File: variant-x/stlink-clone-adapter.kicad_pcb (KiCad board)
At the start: 2 copper layers, 25.4 x 15 mm, 5 parts, among them J1 Conn_01x04, J2 Conn_01x04, J3 2X5_HDR, J4 Conn_01x04, J5 ARM_10PIN

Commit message: variant-x plot done
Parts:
- added D1: LED, LED_SMD:LED_0603_1608Metric, F.Cu at (141.5, 117.9)
- added R1: R, Resistor_SMD:R_0603_1608Metric, F.Cu at (145.5, 117.8)
- added REF**: snowflake, project-lib:snowflake, F.Cu at (143.3, 115.3)
- moved J5 5.72 mm to (151.8, 110.5)
- moved J1 5.46 mm to (141.0, 106.7)
- moved J2 5.34 mm to (143.5, 106.7)
- moved J4 5.34 mm to (146.1, 106.7)
- moved J3 4.18 mm to (119.4, 105.4)
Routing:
- net /3.3V: track 0.00 -> 40.7 mm
- net /RST: track 0.00 -> 24.7 mm
- net /SWDIO|SWCLK: track 0.00 -> 22.6 mm
- net /GND: track 1.27 -> 21.4 mm, vias 0 -> 2
- net /GND|SWIM: track 0.00 -> 17.5 mm
- net /SWCLK: track 0.00 -> 15.6 mm
- net /GND|SWDIO: track 0.00 -> 15.5 mm
- net /SWIM: track 0.00 -> 14.0 mm
- net /SWIM|GND: track 0.00 -> 13.0 mm
- net /SWDIO: track 0.00 -> 10.8 mm
- net /SWCLK|GND: track 0.00 -> 10.5 mm
- net Net-(D1-Pad1): track 0.00 -> 2.45 mm
- added copper zone on F.Cu, net (none)
- added copper zone on B.Cu, net /GND
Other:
- board size 25.4 x 15 mm -> 25.1 x 18 mm
- board text added: "+3.3V"

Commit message: note for jumper
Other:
- board text added: "1"
- board text added: "2"

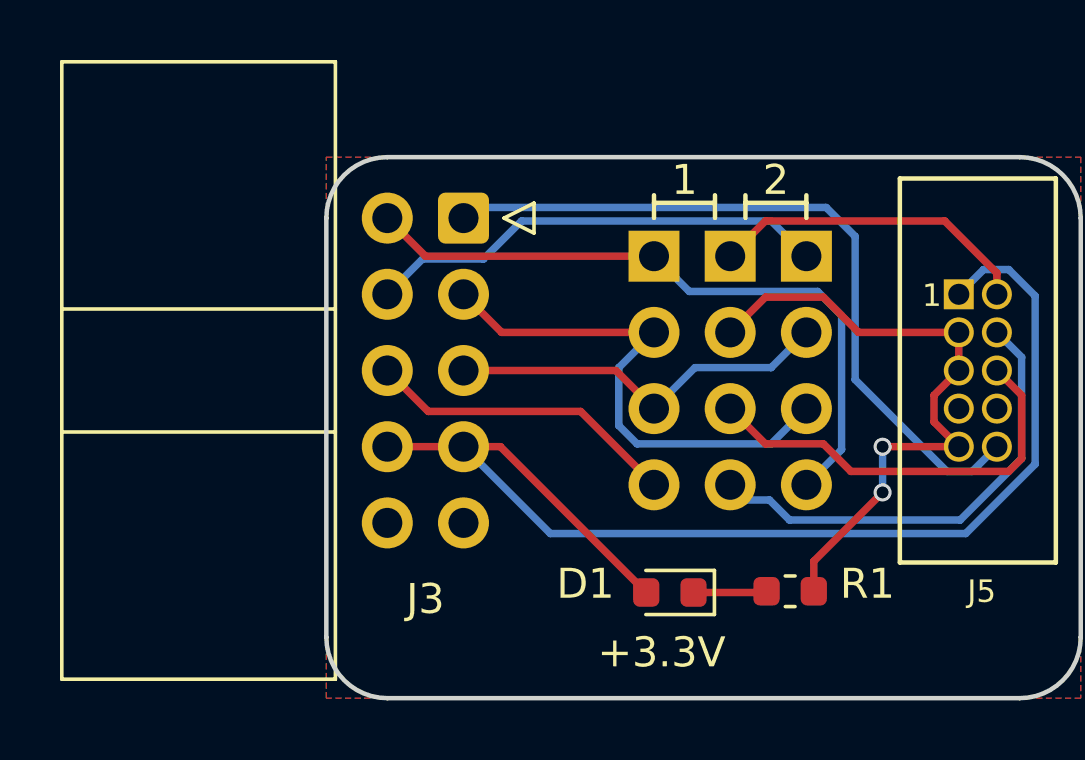
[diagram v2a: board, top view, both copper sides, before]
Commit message: fix 2x5 header
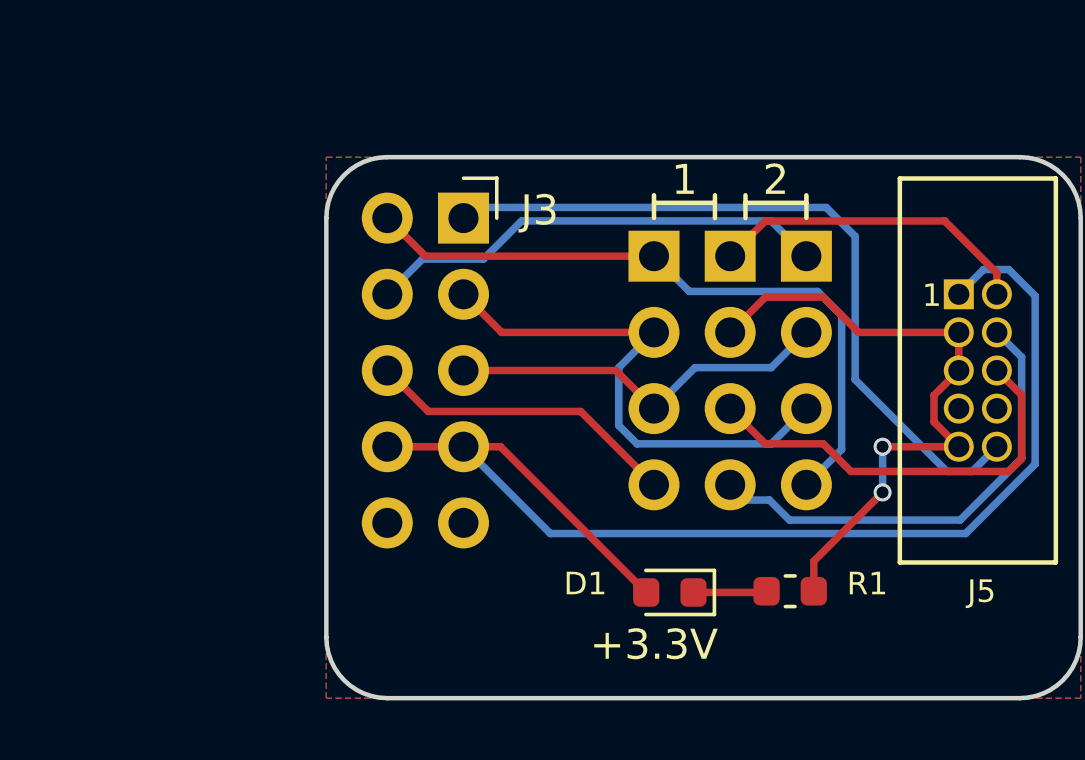
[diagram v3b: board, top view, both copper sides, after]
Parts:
- J3: footprint project-lib:IDC-Header_2x05_P2.54mm_Horizontal -> Connector_PinSocket_2.54mm:PinSocket_2x05_P2.54mm_Horizontal
- moved J3 15.2 mm to (134.6, 105.4)

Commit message: kibot
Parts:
- J3: value 2X5_HDR -> Conn_02x05_Odd_Even
- J5: value ARM_10PIN -> Conn_ARM_JTAG_SWD_10
- R1: value R -> 1K
- moved REF** 0.38 mm to (143.3, 115.7)
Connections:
- net /3.3V renamed /+3.3V
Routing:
- net /GND: vias 2 -> 3

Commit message: add example 2x4 jumper
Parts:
- added REF**: 2x4_jumper_shunt_3d_only, project-lib:2x4_jumper_shunt_3d_only, F.Cu at (141.0, 106.7)

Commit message: wip
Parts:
- removed the J2 at (143.5, 106.7)
- removed J4: Conn_01x04, project-lib:PinHeader_1x04_P2.54mm_Vertical
- removed REF**: 2x4_jumper_shunt_3d_only, project-lib:2x4_jumper_shunt_3d_only
- removed REF**: snowflake, project-lib:snowflake
- J1: value Conn_01x04 -> Conn_02x05_Odd_Even; footprint project-lib:PinHeader_1x04_P2.54mm_Vertical -> Connector_PinSocket_2.54mm:PinSocket_2x05_P2.54mm_Horizontal
- moved D1 30.7 mm to (136.9, 87.5)
- moved R1 30.7 mm to (140.9, 87.5)
- moved J2 27.5 mm to (133.0, 78.0), turned to 315 degrees
- moved J3 22.9 mm to (151.4, 87.6)
- moved J1 22.4 mm to (125.7, 90.3), turned to 45 degrees
- renumbered J3 to J2, J5 to J3
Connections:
- J1 pad 1: /SWDIO|SWCLK -> /RST
- J1 pad 2: /GND|SWIM -> /SWCLK
- J1 pad 3: /SWIM|GND -> /SWIM
- J1 pad 4: /SWCLK|GND -> /SWDIO
- J2 pad 2: /SWDIO|SWCLK -> /SWDIO
- J2 pad 3: /GND|SWIM -> /GND
- J2 pad 4: /GND|SWDIO -> /GND
- J2 pad 5: /SWIM|GND -> /SWIM
- J2 pad 6: /SWCLK|GND -> /SWCLK
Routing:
- net /+3.3V: track 40.7 -> 0.00 mm
- net /RST: track 24.7 -> 0.00 mm
- net /SWDIO|SWCLK: track 22.6 -> 0.00 mm
- net /GND: track 21.4 -> 0.00 mm, vias 3 -> 0
- net /GND|SWIM: track 17.5 -> 0.00 mm
- net /SWCLK: track 15.6 -> 0.00 mm
- net /GND|SWDIO: track 15.5 -> 0.00 mm
- net /SWIM: track 14.0 -> 0.00 mm
- net /SWIM|GND: track 13.0 -> 0.00 mm
- net /SWDIO: track 10.8 -> 0.00 mm
- net /SWCLK|GND: track 10.5 -> 0.00 mm
- net Net-(D1-Pad1): track 2.45 -> 0.00 mm
- removed copper zone on F.Cu, net (none)
- removed copper zone on B.Cu, net /GND
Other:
- board size 25.1 x 18 mm -> 7.4 x 6.5 mm
- board text removed: "1"
- board text removed: "2"
